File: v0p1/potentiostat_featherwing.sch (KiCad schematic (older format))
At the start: 16 parts, among them J1 Screw_Terminal_01x03, P1 pin_array_3x1, U1 feather_wing, U2 LMP7721, U3 LMP7721, U4 LMP7721, U5 LMP7721

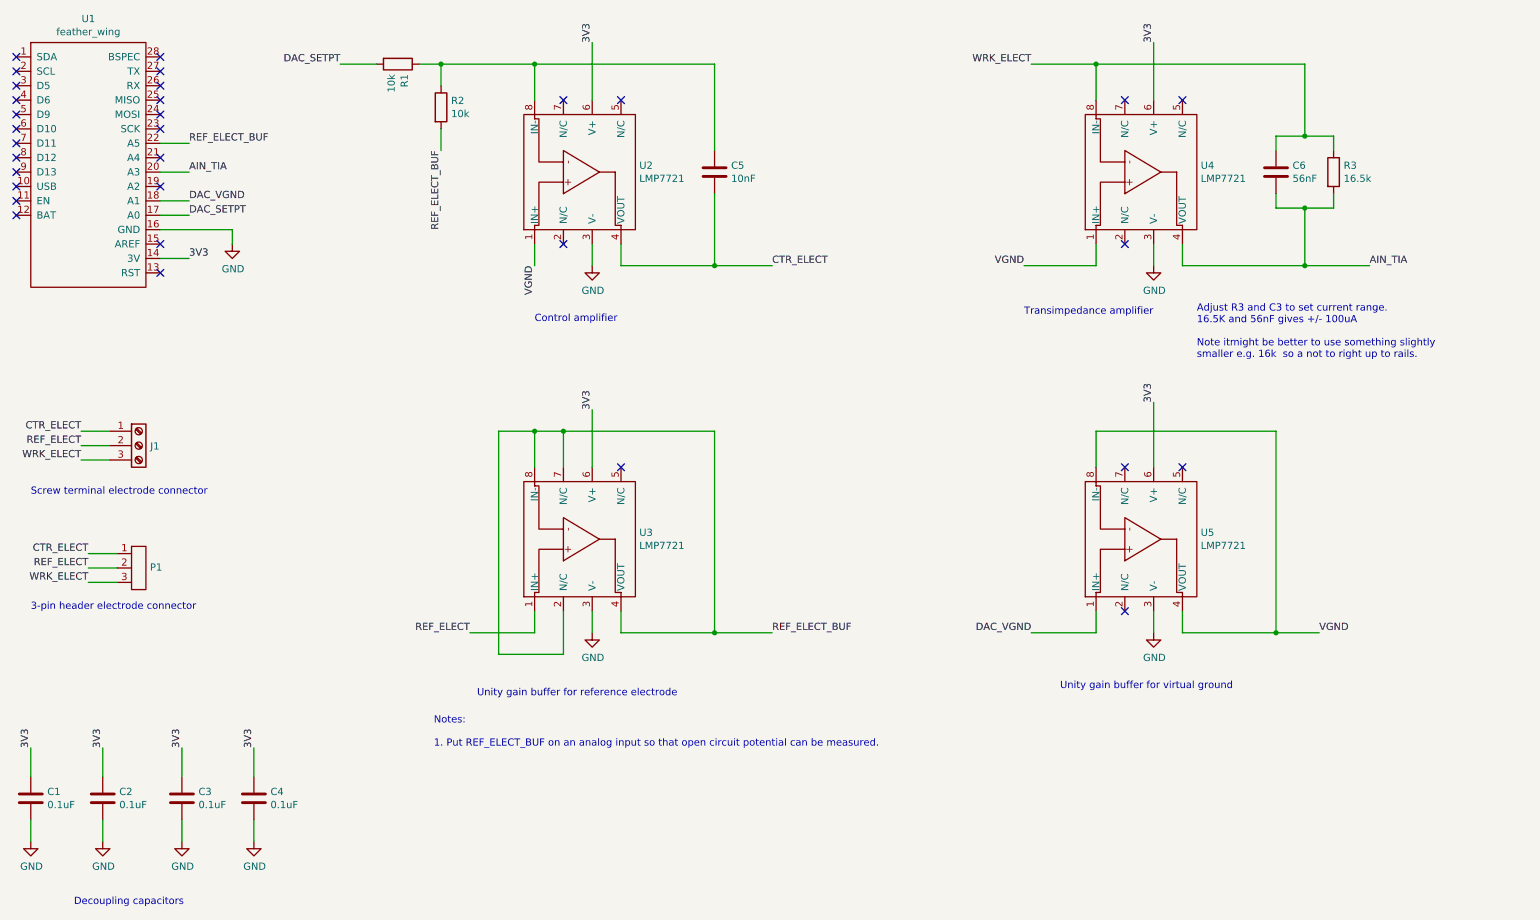
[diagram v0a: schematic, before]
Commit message: Added new v0.2 version of the featherwing design.
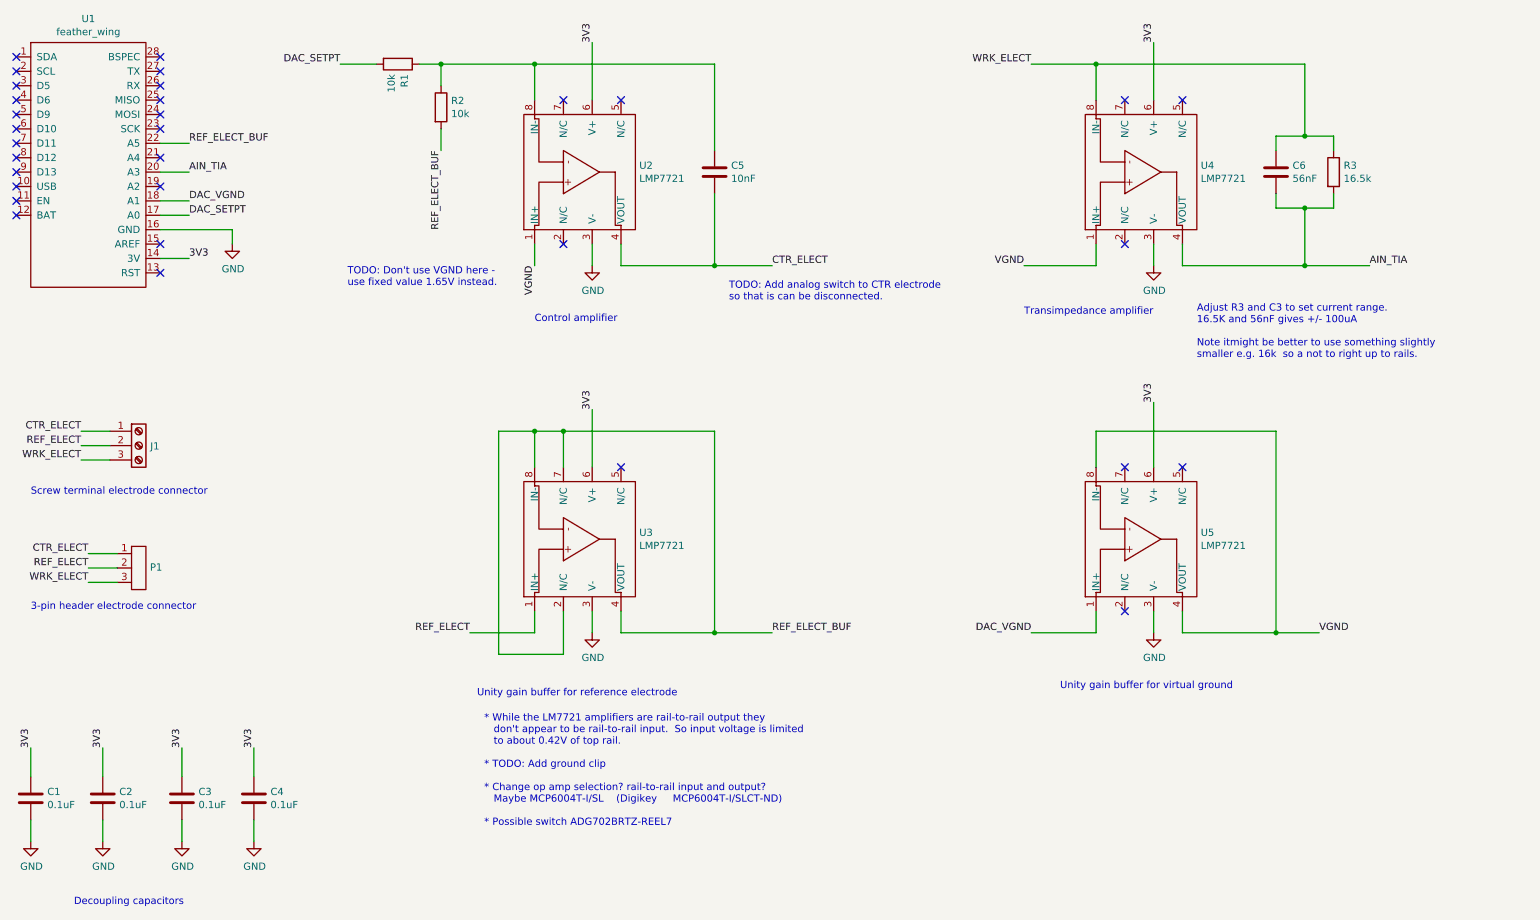
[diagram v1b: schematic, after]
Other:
- note added: "* While the LM7721 amplifiers are rail-to-rail output they \n don't appear to be rail-to-rail input. So input voltage is limited \n to about 0.42V of top rail. \n\n* TODO: Add ground clip\n\n* Change op amp selection? rail-to-rail input and output? \n Maybe MCP6004T-I/SL (Digikey MCP6004T-I/SLCT-ND)\n\n* Possible switch ADG702BRTZ-REEL7 \n"
- note added: "TODO: Add analog switch to CTR electrode \nso that is can be disconnected."
- note added: "TODO: Don't use VGND here - \nuse fixed value 1.65V instead."
- note removed: "Notes:\n\n1. Put REF_ELECT_BUF on an analog input so that open circuit potential can be measured."
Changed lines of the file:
@@
 Wire Wire Line
 	4850 4750 4850 5050
-Text Notes 3950 5700 0    50   ~ 0
-Notes:\n\n1. Put REF_ELECT_BUF on an analog input so that open circuit potential can be measured.
 NoConn ~ 2050 1600
 Wire Wire Line
@@
 Text Label 2250 1500 0    50   ~ 0
 REF_ELECT_BUF
+Text Notes 3350 2500 0    50   ~ 0
+TODO: Don't use VGND here - \nuse fixed value 1.65V instead.
+Text Notes 6000 2600 0    50   ~ 0
+TODO: Add analog switch to CTR electrode \nso that is can be disconnected.
+Text Notes 4300 6250 0    50   ~ 0
+* While the LM7721 amplifiers are rail-to-rail output they \n   don't appear to be rail-to-rail input.  So input voltage is limited \n   to about 0.42V of top rail. \n\n* TODO: Add ground clip\n\n* Change op amp selection? rail-to-rail input and output?  \n   Maybe MCP6004T-I/SL    (Digikey 	MCP6004T-I/SLCT-ND)\n\n* Possible switch ADG702BRTZ-REEL7  \n
 $EndSCHEMATC
